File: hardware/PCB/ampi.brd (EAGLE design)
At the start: 56 x 67.9 mm, 41 parts, among them K1 NA, K2 NA, Q1 BSS138, U2 RASPBERRY_PI_3_MODEL_B+

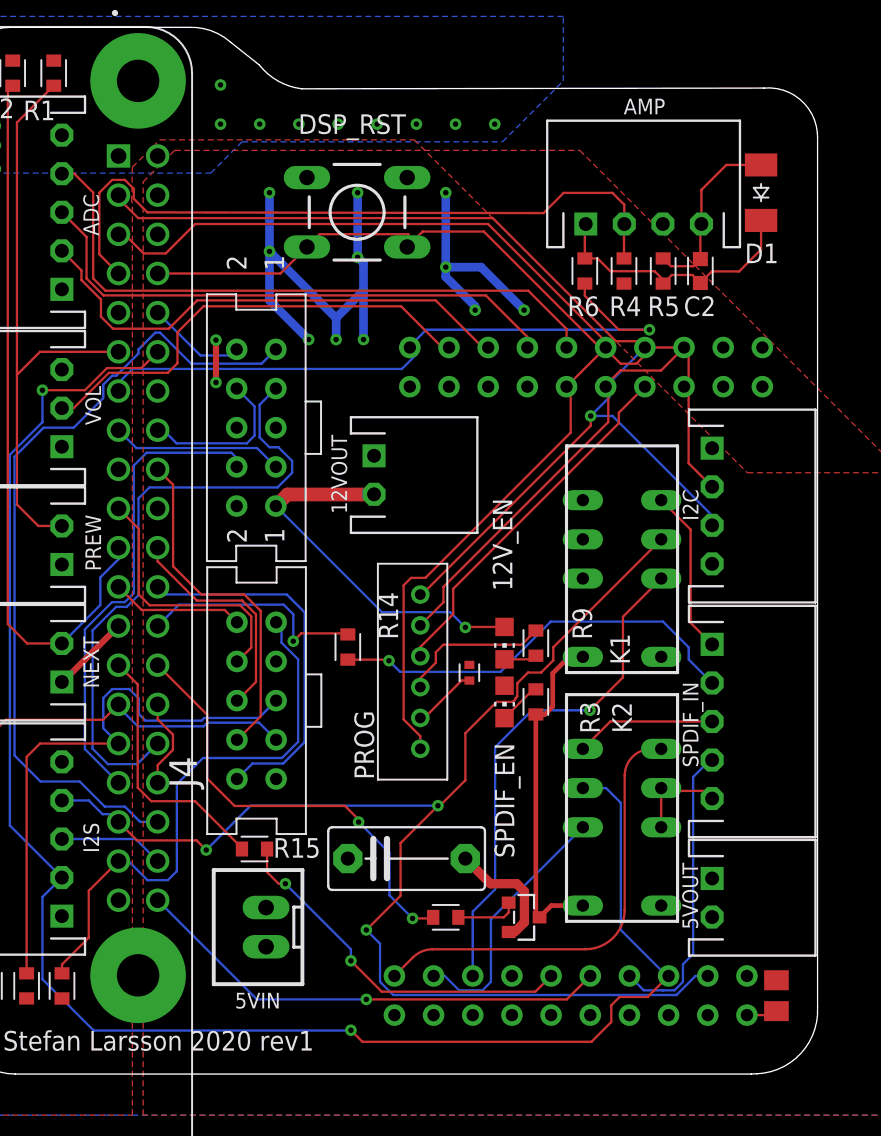
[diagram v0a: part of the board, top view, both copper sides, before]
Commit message: fix pinout and temp_controller test
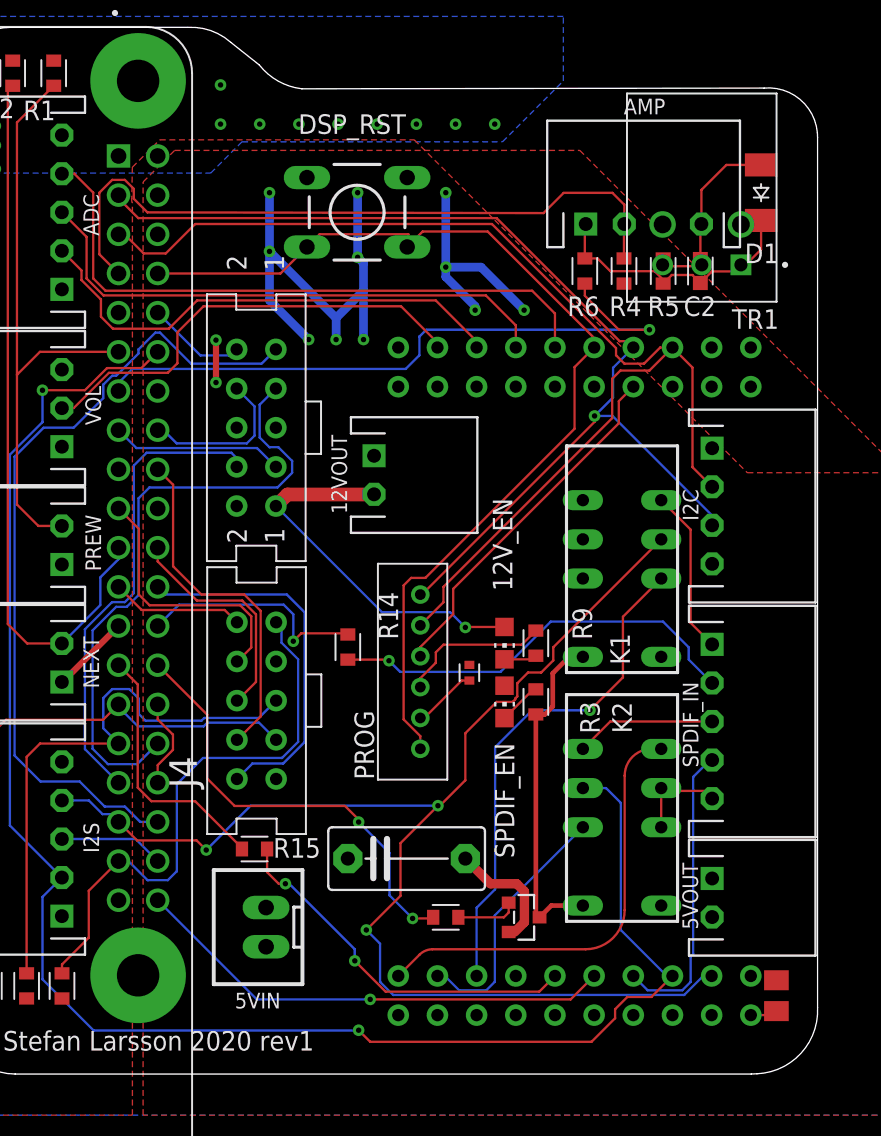
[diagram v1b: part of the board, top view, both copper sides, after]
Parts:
- added TR1: PLT133/T10W, PLT133_T10W:XDCR_PLT133/T10W
- moved J1 0.75 mm to (33.8, 56.0)
- moved J2 0.25 mm to (33.8, 15.2)
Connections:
- new net VCC: TR1.2
- net GND: now also TR1.3
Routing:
- net SDA: track 71.6 -> 70.3 mm
- net SCL: track 78.9 -> 77.7 mm
- net DSP_RST: track 67.0 -> 66.3 mm
- net ADC_VOL: track 30.1 -> 29.6 mm
- net ADC3: track 32.8 -> 32.3 mm
